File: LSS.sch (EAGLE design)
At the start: 16 parts, among them J1 Digital_0_7, J2 Analog, J3 Digital_8_13

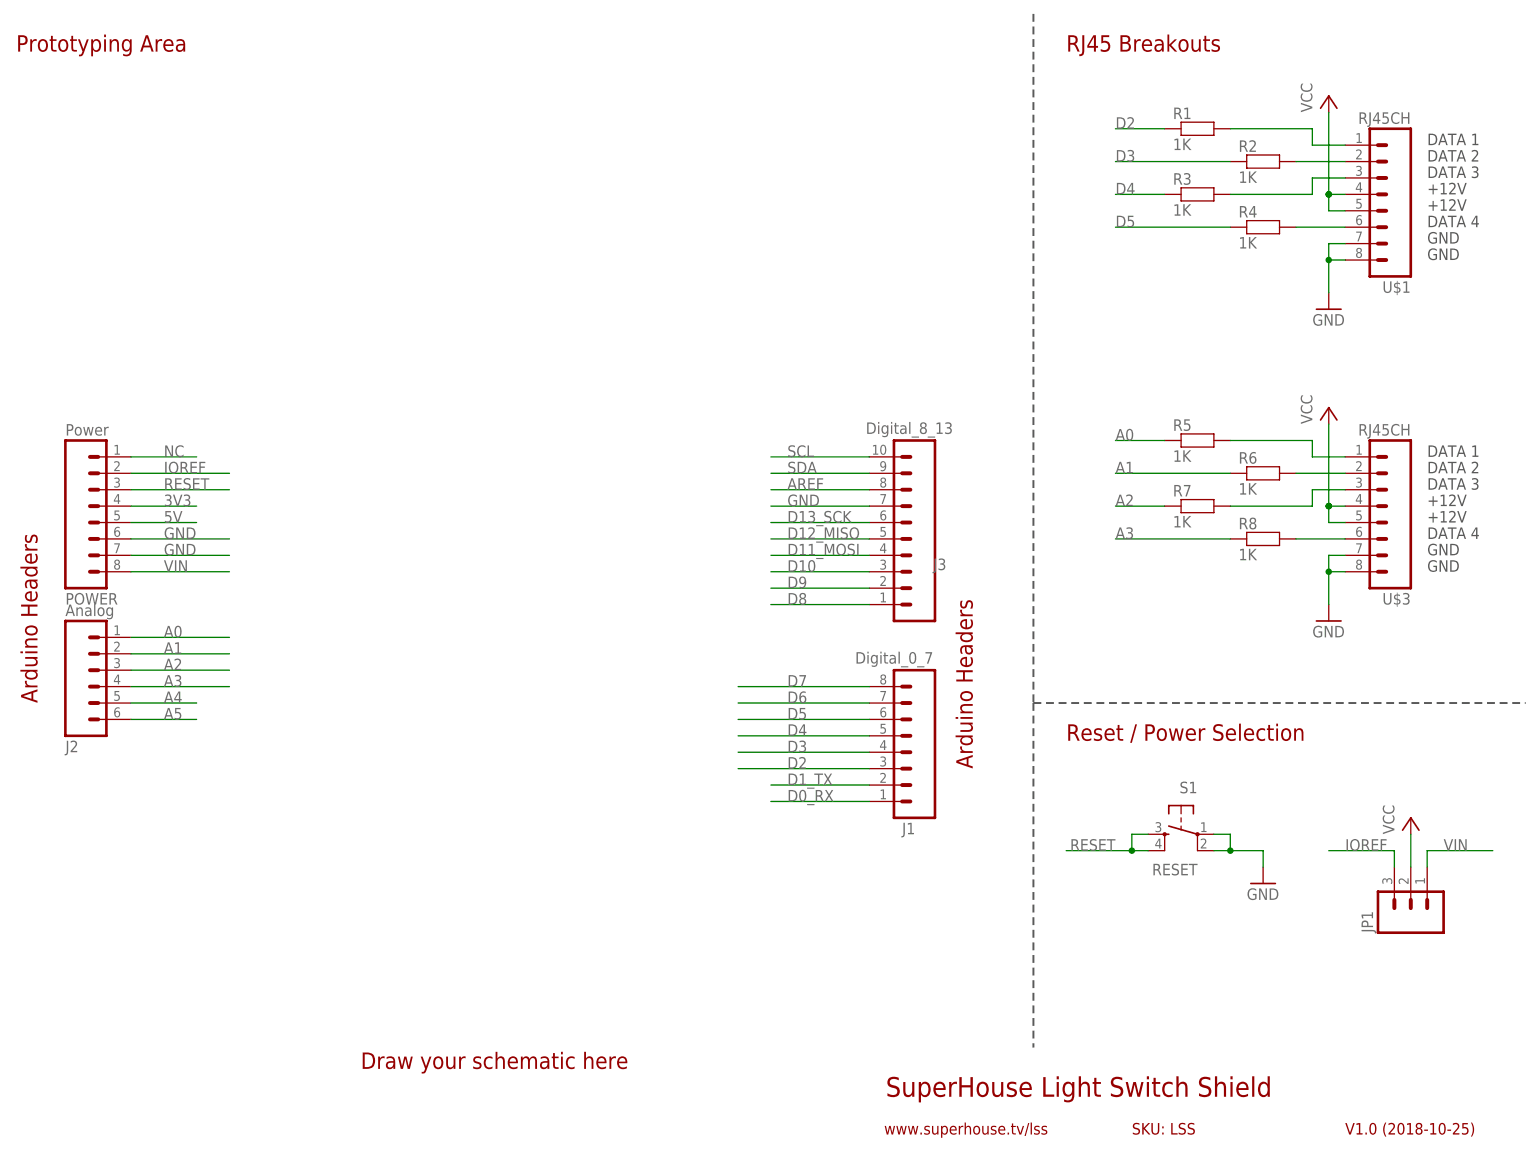
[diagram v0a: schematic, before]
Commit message: Release v1.1 with D4 cleared to allow use on EtherTen
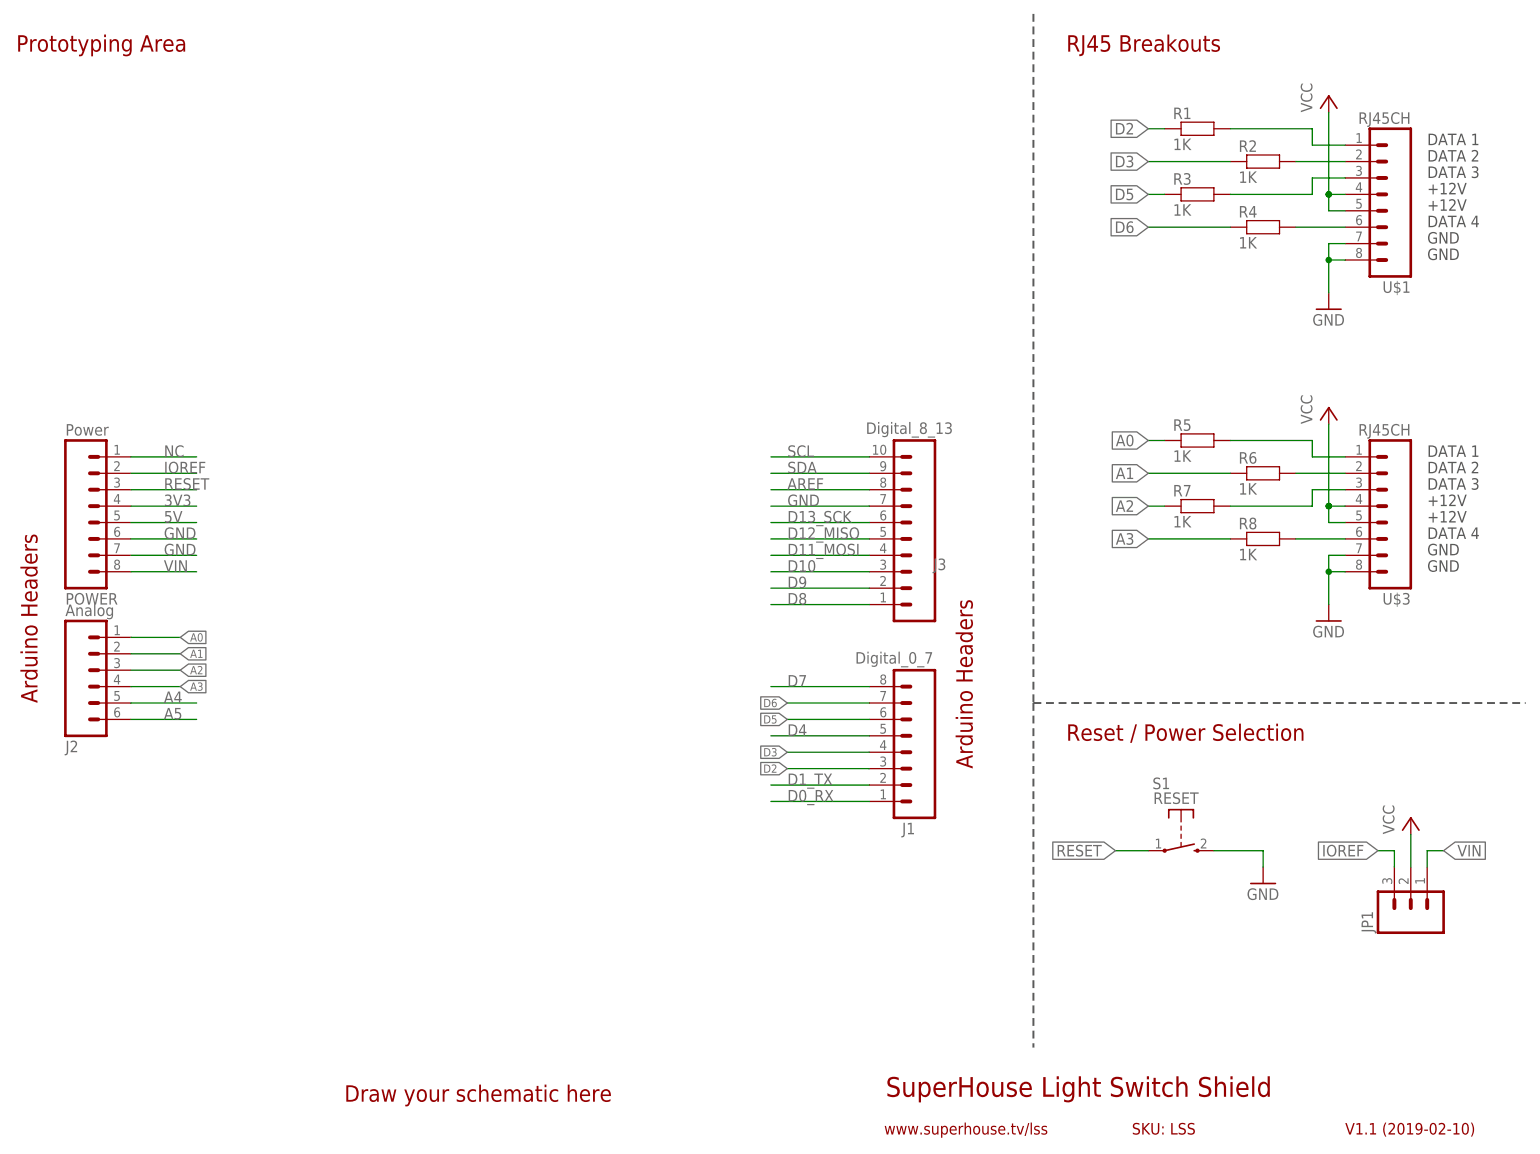
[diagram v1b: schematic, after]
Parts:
- S1: device freetronics:TAC_SWITCHPTH -> freetronics-jon:TAC_SWITCH_2PINSMT
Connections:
- net D4: no longer R3.1
- net D5: now also R3.1; no longer R4.1
- net D6: now also R4.1
- net GND: now also S1.S; no longer S1.1, S1.2
- net RESET: now also S1.P; no longer S1.3, S1.4
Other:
- note added: "V1.1 (2019-02-10)"
- note removed: "V1.0 (2018-10-25)"
